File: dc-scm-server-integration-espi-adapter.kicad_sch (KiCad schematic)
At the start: 10 parts

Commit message: chore: set date and project name
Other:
- title: DC-SCM Server Integration eSPI Adapter HW -> eSPI Adapter
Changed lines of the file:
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@@
 	(paper "A4")
 	(title_block
-		(title "DC-SCM Server Integration eSPI Adapter HW")
+		(title "eSPI Adapter")
 		(date "2026-08-21")
 		(rev "1.0.0")
 		(company "Antmicro")
-		(comment 1 "www.antmicro.com")
 	)
 	(bus

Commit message: [#103224] Initial placement/visualization
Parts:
- added H1001, H1002, H1003, H1004: Spacer_Drill4.4mm_H6mm_9774060360R, antmicro-footprints:Spacer_Drill4.4mm_H6mm_9774060360R, symbol MechanicalParts:Spacer_Drill4.4mm_H6mm_9774060360R
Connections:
- new net GND: H1001.1, H1002.1, H1003.1, H1004.1
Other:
- moved on the sheet: N1001, N1002

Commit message: [#103696] Initial placement of all components, delete redundant testpoints
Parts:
- N1001: footprint antmicro-footprints:antmicro-logo -> antmicro-footprints:antmicro-logo_scaled_12mm
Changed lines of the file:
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@@
 			)
 		)
-		(property "Footprint" "antmicro-footprints:antmicro-logo"
+		(property "Footprint" "antmicro-footprints:antmicro-logo_scaled_12mm"
 			(at 240.03 176.53 0)
 			(hide yes)

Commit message: [#103696] Implementing changes from review onto PCB
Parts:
- removed FD1006: Fiducial_1mm_Mask2mm, antmicro-footprints:Fiducial_1mm_Mask2mm, symbol Antmicro Symbols:Fiducial_1mm_Mask2mm
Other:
- moved on the sheet: FD1001, FD1002, FD1003, FD1004, FD1005
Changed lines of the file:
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@@
 	(symbol
 		(lib_id "Antmicro Symbols:Fiducial_1mm_Mask2mm")
-		(at 255.27 149.86 0)
+		(at 255.27 157.48 0)
 		(unit 1)
 		(body_style 1)
@@
 		(fields_autoplaced yes)
 		(property "Reference" "FD1005"
-			(at 259.08 148.59 0)
+			(at 259.08 156.21 0)
 			(show_name no)
 			(do_not_autoplace no)
@@
 		)
 		(property "Value" "Fiducial_1mm_Mask2mm"
-			(at 259.08 151.13 0)
+			(at 259.08 158.75 0)
 			(show_name no)
 			(do_not_autoplace no)
@@
 		)
 		(property "Footprint" "antmicro-footprints:Fiducial_1mm_Mask2mm"
-			(at 264.16 154.94 0)
+			(at 264.16 162.56 0)
 			(hide yes)
 			(show_name no)
@@
 		)
 		(property "Datasheet" ""
-			(at 264.49 160.35 0)
+			(at 264.49 167.97 0)
 			(hide yes)
 			(show_name no)
@@
 		)
 		(property "Description" "Fiducial mask"
-			(at 264.49 162.89 0)
+			(at 264.49 170.51 0)
 			(hide yes)
 			(show_name no)
@@
 		)
 		(property "Author" "Antmicro"
-			(at 264.16 157.48 0)
+			(at 264.16 165.1 0)
 			(hide yes)
 			(show_name no)
@@
 		)
 		(property "License" "Apache-2.0"
-			(at 264.16 160.02 0)
+			(at 264.16 167.64 0)
 			(hide yes)
 			(show_name no)
@@
 	(symbol
 		(lib_id "Antmicro Symbols:Fiducial_1mm_Mask2mm")
-		(at 255.27 157.48 0)
-		(unit 1)
-		(body_style 1)
-		(exclude_from_sim no)
-		(in_bom no)
-		(on_board yes)
-		(in_pos_files yes)
-		(dnp no)
-		(fields_autoplaced yes)
-		(property "Reference" "FD1006"
-			(at 259.08 156.21 0)
-			(show_name no)
-			(do_not_autoplace no)
-			(effects
-				(font
-					(size 1.27 1.27)
-					(thickness 0.15)
-				)
-				(justify left)
-			)
-		)
-		(property "Value" "Fiducial_1mm_Mask2mm"
-			(at 259.08 158.75 0)
-			(show_name no)
-			(do_not_autoplace no)
-			(effects
-				(font
-					(size 1.27 1.27)
-					(thickness 0.15)
-				)
-				(justify left)
-			)
-		)
-		(property "Footprint" "antmicro-footprints:Fiducial_1mm_Mask2mm"
-			(at 264.16 162.56 0)
-			(hide yes)
-			(show_name no)
-			(do_not_autoplace no)
-			(effects
-				(font
-					(size 1.27 1.27)
-					(thickness 0.15)
-				)
-				(justify left bottom)
-			)
-		)
-		(property "Datasheet" ""
-			(at 264.49 167.97 0)
-			(hide yes)
-			(show_name no)
-			(do_not_autoplace no)
-			(effects
-				(font
-					(size 1.27 1.27)
-					(thickness 0.15)
-				)
-				(justify left bottom)
-			)
-		)
-		(property "Description" "Fiducial mask"
-			(at 264.49 170.51 0)
-			(hide yes)
-			(show_name no)
-			(do_not_autoplace no)
-			(effects
-				(font
-					(size 1.27 1.27)
-				)
-				(justify left bottom)
-			)
-		)
-		(property "Author" "Antmicro"
-			(at 264.16 165.1 0)
-			(hide yes)
-			(show_name no)
-			(do_not_autoplace no)
-			(effects
-				(font
-					(size 1.27 1.27)
-					(thickness 0.15)
-				)
-				(justify left bottom)
-			)
-		)
-		(property "License" "Apache-2.0"
-			(at 264.16 167.64 0)
-			(hide yes)
-			(show_name no)
-			(do_not_autoplace no)
-			(effects
-				(font
-					(size 1.27 1.27)
-					(thickness 0.15)
-				)
-				(justify left bottom)
-			)
-		)
-		(instances
-			(project "dc-scm-server-integration-espi-adapter"
-				(path "/df391740-647e-4ab6-9dcd-d61184d66fe9"
-					(reference "FD1006")
-					(unit 1)
-				)
-			)
-		)
-	)
-	(symbol
-		(lib_id "Antmicro Symbols:Fiducial_1mm_Mask2mm")
-		(at 255.27 127 0)
+		(at 255.27 134.62 0)
 		(unit 1)
 		(body_style 1)
@@
 		(fields_autoplaced yes)
 		(property "Reference" "FD1002"
-			(at 259.08 125.73 0)
+			(at 259.08 133.35 0)
 			(show_name no)
 			(do_not_autoplace no)
@@
 		)
 		(property "Value" "Fiducial_1mm_Mask2mm"
-			(at 259.08 128.27 0)
+			(at 259.08 135.89 0)
 			(show_name no)
 			(do_not_autoplace no)
@@
 		)
 		(property "Footprint" "antmicro-footprints:Fiducial_1mm_Mask2mm"
-			(at 264.16 132.08 0)
+			(at 264.16 139.7 0)
 			(hide yes)
 			(show_name no)
@@
 		)
 		(property "Datasheet" ""
-			(at 264.49 137.49 0)
+			(at 264.49 145.11 0)
 			(hide yes)
 			(show_name no)
@@
 		)
 		(property "Description" "Fiducial mask"
-			(at 264.49 140.03 0)
+			(at 264.49 147.65 0)
 			(hide yes)
 			(show_name no)
@@
 		)
 		(property "Author" "Antmicro"
-			(at 264.16 134.62 0)
+			(at 264.16 142.24 0)
 			(hide yes)
 			(show_name no)
@@
 		)
 		(property "License" "Apache-2.0"
-			(at 264.16 137.16 0)
+			(at 264.16 144.78 0)
 			(hide yes)
 			(show_name no)
@@
 	(symbol
 		(lib_id "Antmicro Symbols:Fiducial_1mm_Mask2mm")
-		(at 255.27 119.38 0)
+		(at 255.27 127 0)
 		(unit 1)
 		(body_style 1)
@@
 		(fields_autoplaced yes)
 		(property "Reference" "FD1001"
-			(at 259.08 118.11 0)
+			(at 259.08 125.73 0)
 			(show_name no)
 			(do_not_autoplace no)
@@
 		)
 		(property "Value" "Fiducial_1mm_Mask2mm"
-			(at 259.08 120.65 0)
+			(at 259.08 128.27 0)
 			(show_name no)
 			(do_not_autoplace no)
@@
 		)
 		(property "Footprint" "antmicro-footprints:Fiducial_1mm_Mask2mm"
-			(at 264.16 124.46 0)
+			(at 264.16 132.08 0)
 			(hide yes)
 			(show_name no)
@@
 		)
 		(property "Datasheet" ""
-			(at 264.49 129.87 0)
+			(at 264.49 137.49 0)
 			(hide yes)
 			(show_name no)
@@
 		)
 		(property "Description" "Fiducial mask"
-			(at 264.49 132.41 0)
+			(at 264.49 140.03 0)
 			(hide yes)
 			(show_name no)
@@
 		)
 		(property "Author" "Antmicro"
-			(at 264.16 127 0)
+			(at 264.16 134.62 0)
 			(hide yes)
 			(show_name no)
@@
 		)
 		(property "License" "Apache-2.0"
-			(at 264.16 129.54 0)
+			(at 264.16 137.16 0)
 			(hide yes)
 			(show_name no)
@@
 	(symbol
 		(lib_id "Antmicro Symbols:Fiducial_1mm_Mask2mm")
-		(at 255.27 134.62 0)
+		(at 255.27 142.24 0)
 		(unit 1)
 		(body_style 1)
@@
 		(fields_autoplaced yes)
 		(property "Reference" "FD1003"
-			(at 259.08 133.35 0)
+			(at 259.08 140.97 0)
 			(show_name no)
 			(do_not_autoplace no)
@@
 		)
 		(property "Value" "Fiducial_1mm_Mask2mm"
-			(at 259.08 135.89 0)
+			(at 259.08 143.51 0)
 			(show_name no)
 			(do_not_autoplace no)
@@
 		)
 		(property "Footprint" "antmicro-footprints:Fiducial_1mm_Mask2mm"
-			(at 264.16 139.7 0)
+			(at 264.16 147.32 0)
 			(hide yes)
 			(show_name no)
@@
 		)
 		(property "Datasheet" ""
-			(at 264.49 145.11 0)
+			(at 264.49 152.73 0)
 			(hide yes)
 			(show_name no)
@@
 		)
 		(property "Description" "Fiducial mask"
-			(at 264.49 147.65 0)
+			(at 264.49 155.27 0)
 			(hide yes)
 			(show_name no)
@@
 		)
 		(property "Author" "Antmicro"
-			(at 264.16 142.24 0)
+			(at 264.16 149.86 0)
 			(hide yes)
 			(show_name no)
@@
 		)
 		(property "License" "Apache-2.0"
-			(at 264.16 144.78 0)
+			(at 264.16 152.4 0)
 			(hide yes)
 			(show_name no)
@@
 	(symbol
 		(lib_id "Antmicro Symbols:Fiducial_1mm_Mask2mm")
-		(at 255.27 142.24 0)
+		(at 255.27 149.86 0)
 		(unit 1)
 		(body_style 1)
@@
 		(fields_autoplaced yes)
 		(property "Reference" "FD1004"
-			(at 259.08 140.97 0)
+			(at 259.08 148.59 0)
 			(show_name no)
 			(do_not_autoplace no)
@@
 		)
 		(property "Value" "Fiducial_1mm_Mask2mm"
-			(at 259.08 143.51 0)
+			(at 259.08 151.13 0)
 			(show_name no)
 			(do_not_autoplace no)
@@
 		)
 		(property "Footprint" "antmicro-footprints:Fiducial_1mm_Mask2mm"
-			(at 264.16 147.32 0)
+			(at 264.16 154.94 0)
 			(hide yes)
 			(show_name no)
@@
 		)
 		(property "Datasheet" ""
-			(at 264.49 152.73 0)
+			(at 264.49 160.35 0)
 			(hide yes)
 			(show_name no)
@@
 		)
 		(property "Description" "Fiducial mask"
-			(at 264.49 155.27 0)
+			(at 264.49 162.89 0)
 			(hide yes)
 			(show_name no)
@@
 		)
 		(property "Author" "Antmicro"
-			(at 264.16 149.86 0)
+			(at 264.16 157.48 0)
 			(hide yes)
 			(show_name no)
@@
 		)
 		(property "License" "Apache-2.0"
-			(at 264.16 152.4 0)
-			(hide yes)
-			(show_name no)
+			(at 264.16 160.02 0)
+			(hide yes)
+			(show_name no)

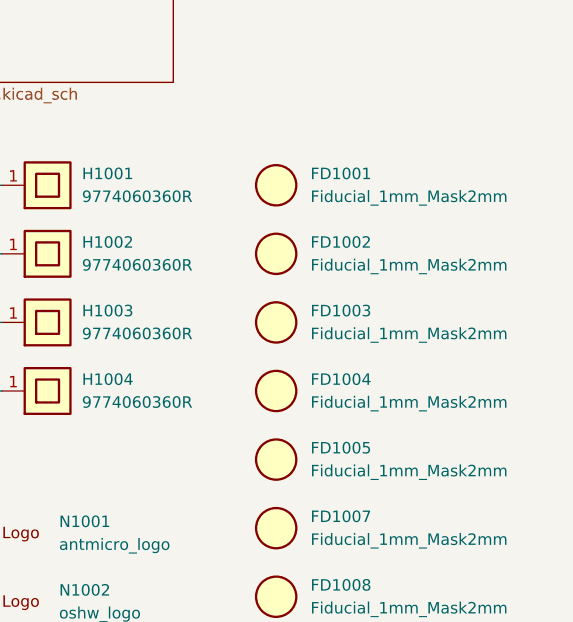
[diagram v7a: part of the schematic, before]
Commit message: [#103696] Change redundant LED connections, place LEDs on PCB
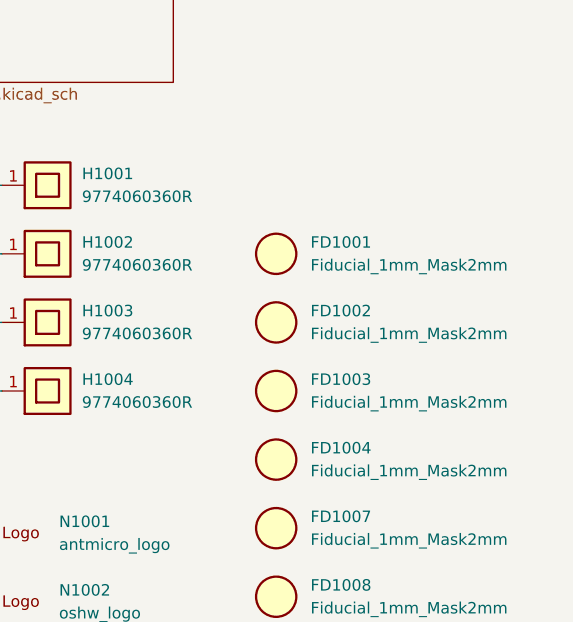
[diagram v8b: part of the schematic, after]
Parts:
- removed FD1005: Fiducial_1mm_Mask2mm, antmicro-footprints:Fiducial_1mm_Mask2mm, symbol Antmicro Symbols:Fiducial_1mm_Mask2mm
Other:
- moved on the sheet: FD1001, FD1002, FD1003, FD1004
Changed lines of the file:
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@@
-	)
-	(symbol
-		(lib_id "Antmicro Symbols:Fiducial_1mm_Mask2mm")
-		(at 255.27 157.48 0)
-		(unit 1)
-		(body_style 1)
-		(exclude_from_sim no)
-		(in_bom no)
-		(on_board yes)
-		(in_pos_files yes)
-		(dnp no)
-		(fields_autoplaced yes)
-		(property "Reference" "FD1005"
-			(at 259.08 156.21 0)
-			(show_name no)
-			(do_not_autoplace no)
-			(effects
-				(font
-					(size 1.27 1.27)
-					(thickness 0.15)
-				)
-				(justify left)
-			)
-		)
-		(property "Value" "Fiducial_1mm_Mask2mm"
-			(at 259.08 158.75 0)
-			(show_name no)
-			(do_not_autoplace no)
-			(effects
-				(font
-					(size 1.27 1.27)
-					(thickness 0.15)
-				)
-				(justify left)
-			)
-		)
-		(property "Footprint" "antmicro-footprints:Fiducial_1mm_Mask2mm"
-			(at 264.16 162.56 0)
-			(hide yes)
-			(show_name no)
-			(do_not_autoplace no)
-			(effects
-				(font
-					(size 1.27 1.27)
-					(thickness 0.15)
-				)
-				(justify left bottom)
-			)
-		)
-		(property "Datasheet" ""
-			(at 264.49 167.97 0)
-			(hide yes)
-			(show_name no)
-			(do_not_autoplace no)
-			(effects
-				(font
-					(size 1.27 1.27)
-					(thickness 0.15)
-				)
-				(justify left bottom)
-			)
-		)
-		(property "Description" "Fiducial mask"
-			(at 264.49 170.51 0)
-			(hide yes)
-			(show_name no)
-			(do_not_autoplace no)
-			(effects
-				(font
-					(size 1.27 1.27)
-				)
-				(justify left bottom)
-			)
-		)
-		(property "Author" "Antmicro"
-			(at 264.16 165.1 0)
-			(hide yes)
-			(show_name no)
-			(do_not_autoplace no)
-			(effects
-				(font
-					(size 1.27 1.27)
-					(thickness 0.15)
-				)
-				(justify left bottom)
-			)
-		)
-		(property "License" "Apache-2.0"
-			(at 264.16 167.64 0)
-			(hide yes)
-			(show_name no)
-			(do_not_autoplace no)
-			(effects
-				(font
-					(size 1.27 1.27)
-					(thickness 0.15)
-				)
-				(justify left bottom)
-			)
-		)
-		(instances
-			(project "dc-scm-server-integration-espi-adapter"
-				(path "/df391740-647e-4ab6-9dcd-d61184d66fe9"
-					(reference "FD1005")
-					(unit 1)
-				)
-			)
-		)
 	)
 	(symbol
@@
 	(symbol
 		(lib_id "Antmicro Symbols:Fiducial_1mm_Mask2mm")
-		(at 255.27 134.62 0)
+		(at 255.27 142.24 0)
 		(unit 1)
 		(body_style 1)
@@
 		(fields_autoplaced yes)
 		(property "Reference" "FD1002"
-			(at 259.08 133.35 0)
+			(at 259.08 140.97 0)
 			(show_name no)
 			(do_not_autoplace no)
@@
 		)
 		(property "Value" "Fiducial_1mm_Mask2mm"
-			(at 259.08 135.89 0)
+			(at 259.08 143.51 0)
 			(show_name no)
 			(do_not_autoplace no)
@@
 		)
 		(property "Footprint" "antmicro-footprints:Fiducial_1mm_Mask2mm"
-			(at 264.16 139.7 0)
+			(at 264.16 147.32 0)
 			(hide yes)
 			(show_name no)
@@
 		)
 		(property "Datasheet" ""
-			(at 264.49 145.11 0)
+			(at 264.49 152.73 0)
 			(hide yes)
 			(show_name no)
@@
 		)
 		(property "Description" "Fiducial mask"
-			(at 264.49 147.65 0)
+			(at 264.49 155.27 0)
 			(hide yes)
 			(show_name no)
@@
 		)
 		(property "Author" "Antmicro"
-			(at 264.16 142.24 0)
+			(at 264.16 149.86 0)
 			(hide yes)
 			(show_name no)
@@
 		)
 		(property "License" "Apache-2.0"
-			(at 264.16 144.78 0)
+			(at 264.16 152.4 0)
 			(hide yes)
 			(show_name no)
@@
 	(symbol
 		(lib_id "Antmicro Symbols:Fiducial_1mm_Mask2mm")
-		(at 255.27 127 0)
+		(at 255.27 134.62 0)
 		(unit 1)
 		(body_style 1)
@@
 		(fields_autoplaced yes)
 		(property "Reference" "FD1001"
-			(at 259.08 125.73 0)
+			(at 259.08 133.35 0)
 			(show_name no)
 			(do_not_autoplace no)
@@
 		)
 		(property "Value" "Fiducial_1mm_Mask2mm"
-			(at 259.08 128.27 0)
+			(at 259.08 135.89 0)
 			(show_name no)
 			(do_not_autoplace no)
@@
 		)
 		(property "Footprint" "antmicro-footprints:Fiducial_1mm_Mask2mm"
-			(at 264.16 132.08 0)
+			(at 264.16 139.7 0)
 			(hide yes)
 			(show_name no)
@@
 		)
 		(property "Datasheet" ""
-			(at 264.49 137.49 0)
+			(at 264.49 145.11 0)
 			(hide yes)
 			(show_name no)
@@
 		)
 		(property "Description" "Fiducial mask"
-			(at 264.49 140.03 0)
+			(at 264.49 147.65 0)
 			(hide yes)
 			(show_name no)
@@
 		)
 		(property "Author" "Antmicro"
-			(at 264.16 134.62 0)
+			(at 264.16 142.24 0)
 			(hide yes)
 			(show_name no)
@@
 		)
 		(property "License" "Apache-2.0"
-			(at 264.16 137.16 0)
+			(at 264.16 144.78 0)
 			(hide yes)
 			(show_name no)
@@
 	(symbol
 		(lib_id "Antmicro Symbols:Fiducial_1mm_Mask2mm")
-		(at 255.27 142.24 0)
+		(at 255.27 149.86 0)
 		(unit 1)
 		(body_style 1)
@@
 		(fields_autoplaced yes)
 		(property "Reference" "FD1003"
-			(at 259.08 140.97 0)
+			(at 259.08 148.59 0)
 			(show_name no)
 			(do_not_autoplace no)
@@
 		)
 		(property "Value" "Fiducial_1mm_Mask2mm"
-			(at 259.08 143.51 0)
+			(at 259.08 151.13 0)
 			(show_name no)
 			(do_not_autoplace no)
@@
 		)
 		(property "Footprint" "antmicro-footprints:Fiducial_1mm_Mask2mm"
-			(at 264.16 147.32 0)
+			(at 264.16 154.94 0)
 			(hide yes)
 			(show_name no)
@@
 		)
 		(property "Datasheet" ""
-			(at 264.49 152.73 0)
+			(at 264.49 160.35 0)
 			(hide yes)
 			(show_name no)
@@
 		)
 		(property "Description" "Fiducial mask"
-			(at 264.49 155.27 0)
+			(at 264.49 162.89 0)
 			(hide yes)
 			(show_name no)
@@
 		)
 		(property "Author" "Antmicro"
-			(at 264.16 149.86 0)
+			(at 264.16 157.48 0)
 			(hide yes)
 			(show_name no)
@@
 		)
 		(property "License" "Apache-2.0"
-			(at 264.16 152.4 0)
+			(at 264.16 160.02 0)
 			(hide yes)
 			(show_name no)
@@
 	(symbol
 		(lib_id "Antmicro Symbols:Fiducial_1mm_Mask2mm")
-		(at 255.27 149.86 0)
+		(at 255.27 157.48 0)
 		(unit 1)
 		(body_style 1)
@@
 		(fields_autoplaced yes)
 		(property "Reference" "FD1004"
-			(at 259.08 148.59 0)
+			(at 259.08 156.21 0)
 			(show_name no)
 			(do_not_autoplace no)
@@
 		)
 		(property "Value" "Fiducial_1mm_Mask2mm"
-			(at 259.08 151.13 0)
+			(at 259.08 158.75 0)
 			(show_name no)
 			(do_not_autoplace no)
@@
 		)
 		(property "Footprint" "antmicro-footprints:Fiducial_1mm_Mask2mm"
-			(at 264.16 154.94 0)
+			(at 264.16 162.56 0)
 			(hide yes)
 			(show_name no)
@@
 		)
 		(property "Datasheet" ""
-			(at 264.49 160.35 0)
+			(at 264.49 167.97 0)
 			(hide yes)
 			(show_name no)
@@
 		)
 		(property "Description" "Fiducial mask"
-			(at 264.49 162.89 0)
+			(at 264.49 170.51 0)
 			(hide yes)
 			(show_name no)
@@
 		)
 		(property "Author" "Antmicro"
-			(at 264.16 157.48 0)
+			(at 264.16 165.1 0)
 			(hide yes)
 			(show_name no)
@@
 		)
 		(property "License" "Apache-2.0"
-			(at 264.16 160.02 0)
-			(hide yes)
-			(show_name no)
+			(at 264.16 167.64 0)
+			(hide yes)
+			(show_name no)
